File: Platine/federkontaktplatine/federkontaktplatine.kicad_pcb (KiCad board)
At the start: 2 copper layers, 256 x 149 mm, 15 parts, among them J1 Conn_01x07

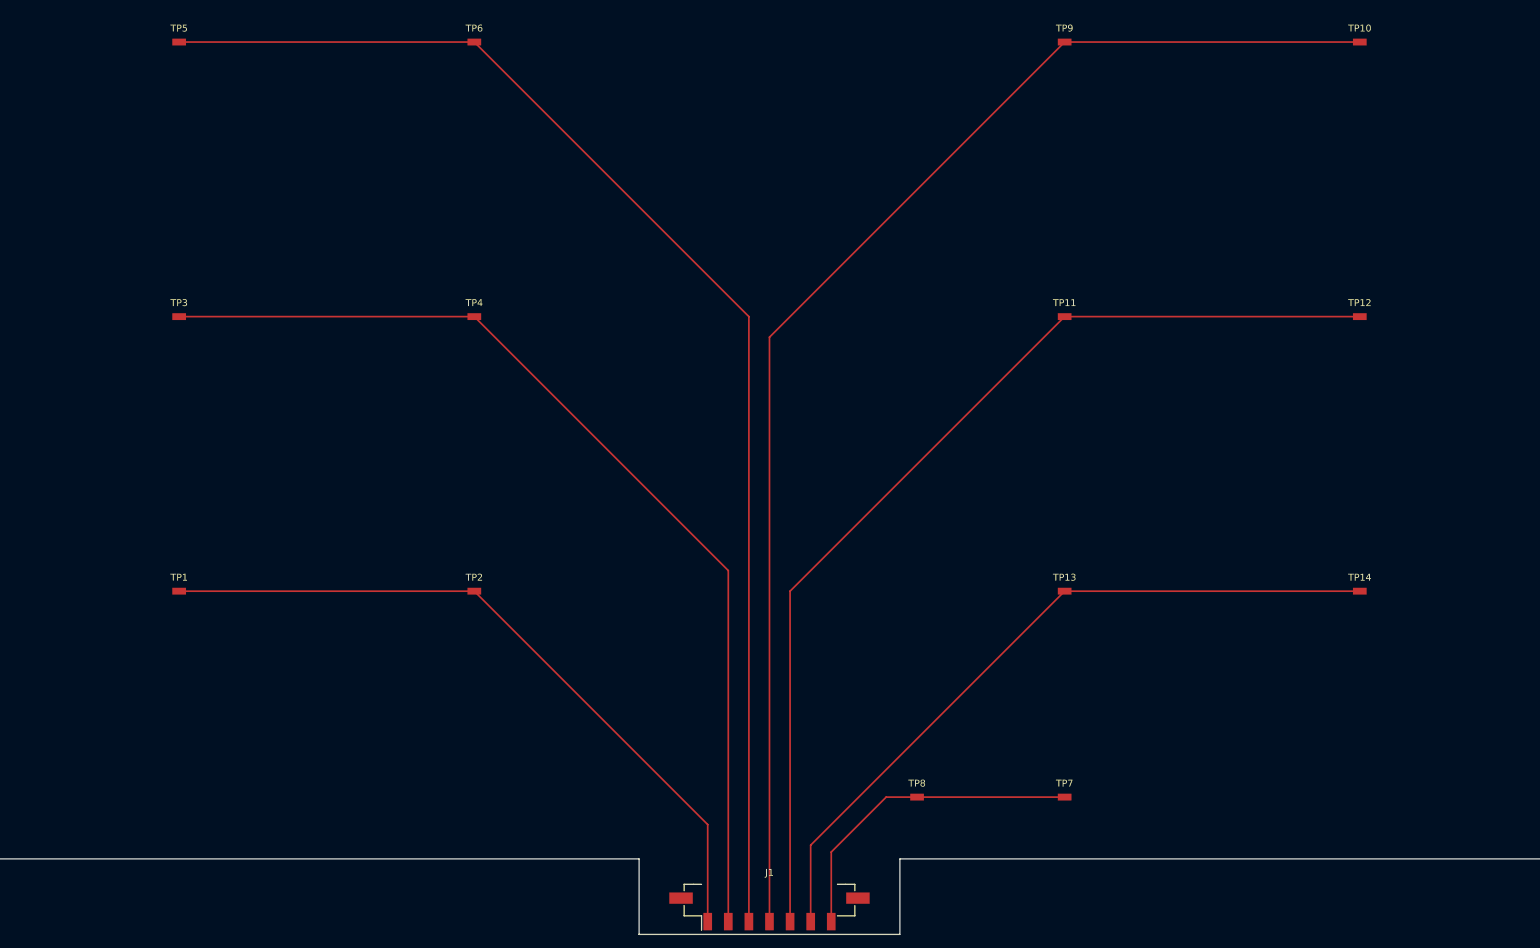
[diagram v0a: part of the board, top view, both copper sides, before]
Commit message: montagepunkte untere platine
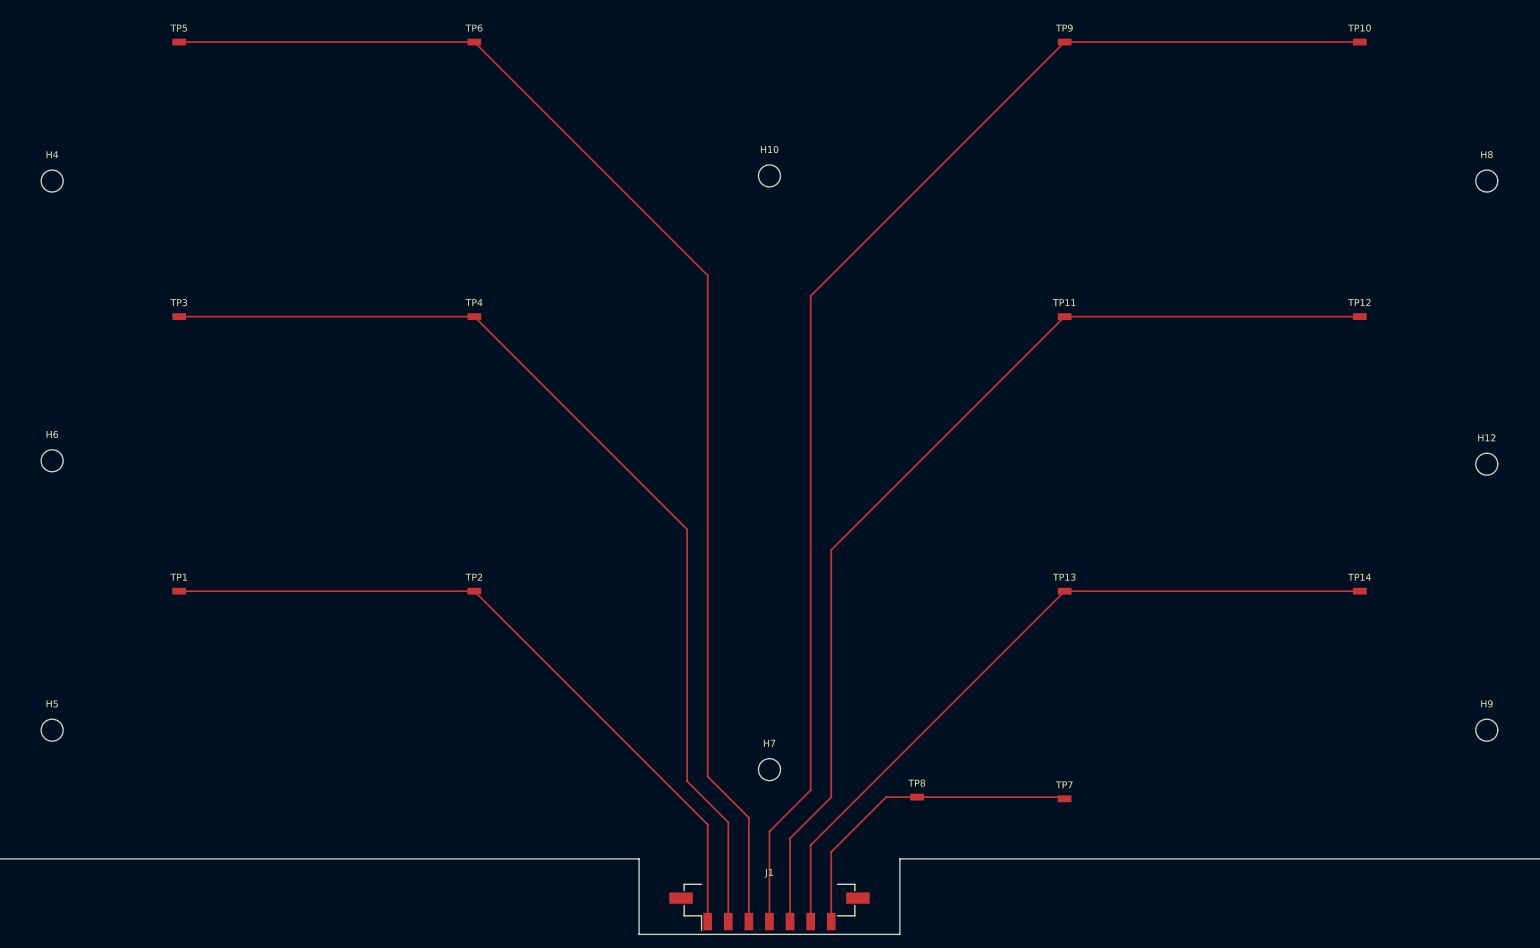
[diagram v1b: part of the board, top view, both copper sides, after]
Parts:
- added H10: MountingHole, MountingHole:MountingHole_3.2mm_M3_DIN965, F.Cu at (148.0, 58.5)
- added H12: MountingHole, MountingHole:MountingHole_3.2mm_M3_DIN965, F.Cu at (252.5, 100.5)
- added H4: MountingHole, MountingHole:MountingHole_3.2mm_M3_DIN965, F.Cu at (43.5, 59.2)
- added H5: MountingHole, MountingHole:MountingHole_3.2mm_M3_DIN965, F.Cu at (43.5, 139.2)
- added H6: MountingHole, MountingHole:MountingHole_3.2mm_M3_DIN965, F.Cu at (43.5, 100.0)
- added H7: MountingHole, MountingHole:MountingHole_3.2mm_M3_DIN965, F.Cu at (148.0, 145.0)
- added H8: MountingHole, MountingHole:MountingHole_3.2mm_M3_DIN965, F.Cu at (252.5, 59.2)
- added H9: MountingHole, MountingHole:MountingHole_3.2mm_M3_DIN965, F.Cu at (252.5, 139.2)
- moved TP7 0.25 mm to (191.0, 149.2)

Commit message: montagelöcher untere platte
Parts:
- added H1: MountingHole, MountingHole:MountingHole_3.2mm_M3_DIN965, F.Cu at (148.0, 19.2)
- added H2: MountingHole, MountingHole:MountingHole_3.2mm_M3_DIN965, F.Cu at (148.0, 99.2)
- moved H7 7.00 mm to (148.0, 138.0)
- moved H12 1.25 mm to (252.5, 99.2)
- moved H10 0.75 mm to (148.0, 59.2)
- moved H6 0.75 mm to (43.5, 99.2)
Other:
- board size 256 x 149 mm -> 256 x 153.8 mm
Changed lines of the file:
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@@
   (net 7 "Net-(J1-Pin_7)")
   (footprint "MountingHole:MountingHole_3.2mm_M3_DIN965" (layer "F.Cu")
-    (at 43.5 100)
+    (at 43.5 99.25)
     (descr "Mounting Hole 3.2mm, no annular, M3, DIN965")
     (tags "mounting hole 3.2mm no annular m3 din965")
@@
     (pad "" np_thru_hole circle (at 0 0) (size 3.2 3.2) (drill 3.2) (layers "*.Cu" "*.Mask"))
   )
+  (footprint "MountingHole:MountingHole_3.2mm_M3_DIN965" (layer "F.Cu")
+    (at 148 99.25)
+    (descr "Mounting Hole 3.2mm, no annular, M3, DIN965")
+    (tags "mounting hole 3.2mm no annular m3 din965")
+    (property "Sheetfile" "federkontaktplatine.kicad_sch")
+    (property "Sheetname" "")
+    (property "ki_description" "Mounting Hole without connection")
+    (property "ki_keywords" "mounting hole")
+    (attr exclude_from_pos_files)
+    (fp_text reference "H2" (at 0 -3.8) (layer "F.SilkS")
+        (effects (font (size 1 1) (thickness 0.15)))
+    )
+    (fp_text value "MountingHole" (at 0 3.8) (layer "F.Fab")
+        (effects (font (size 1 1) (thickness 0.15)))
+    )
+    (fp_text user "${REFERENCE}" (at 0 0) (layer "F.Fab")
+        (effects (font (size 1 1) (thickness 0.15)))
+    )
+    (fp_circle (center 0 0) (end 2.8 0)
+      (stroke (width 0.15) (type solid)) (fill none) (layer "Cmts.User"))
+    (fp_circle (center 0 0) (end 3.05 0)
+      (stroke (width 0.05) (type solid)) (fill none) (layer "F.CrtYd"))
+    (pad "" np_thru_hole circle (at 0 0) (size 3.2 3.2) (drill 3.2) (layers "*.Cu" "*.Mask"))
+  )
   (footprint "TestPoint:PAD_1x2mm" (layer "F.Cu")
     (at 191 79)
@@
   )
   (footprint "MountingHole:MountingHole_3.2mm_M3_DIN965" (layer "F.Cu")
-    (at 148 58.5)
+    (at 148 19.25)
+    (descr "Mounting Hole 3.2mm, no annular, M3, DIN965")
+    (tags "mounting hole 3.2mm no annular m3 din965")
+    (property "Sheetfile" "federkontaktplatine.kicad_sch")
+    (property "Sheetname" "")
+    (property "ki_description" "Mounting Hole without connection")
+    (property "ki_keywords" "mounting hole")
+    (attr exclude_from_pos_files)
+    (fp_text reference "H1" (at 0 4.25) (layer "F.SilkS")
+        (effects (font (size 1 1) (thickness 0.15)))
+    )
+    (fp_text value "MountingHole" (at 0 5.75) (layer "F.Fab")
+        (effects (font (size 1 1) (thickness 0.15)))
+    )
+    (fp_text user "${REFERENCE}" (at 0 0) (layer "F.Fab")
+        (effects (font (size 1 1) (thickness 0.15)))
+    )
+    (fp_circle (center 0 0) (end 2.8 0)
+      (stroke (width 0.15) (type solid)) (fill none) (layer "Cmts.User"))
+    (fp_circle (center 0 0) (end 3.05 0)
+      (stroke (width 0.05) (type solid)) (fill none) (layer "F.CrtYd"))
+    (pad "" np_thru_hole circle (at 0 0) (size 3.2 3.2) (drill 3.2) (layers "*.Cu" "*.Mask"))
+  )
+  (footprint "MountingHole:MountingHole_3.2mm_M3_DIN965" (layer "F.Cu")
+    (at 148 59.25)
     (descr "Mounting Hole 3.2mm, no annular, M3, DIN965")
     (tags "mounting hole 3.2mm no annular m3 din965")
@@
   )
   (footprint "MountingHole:MountingHole_3.2mm_M3_DIN965" (layer "F.Cu")
-    (at 148 145)
+    (at 148 138)
     (descr "Mounting Hole 3.2mm, no annular, M3, DIN965")
     (tags "mounting hole 3.2mm no annular m3 din965")
@@
   )
   (footprint "MountingHole:MountingHole_3.2mm_M3_DIN965" (layer "F.Cu")
-    (at 252.5 100.5)
+    (at 252.5 99.25)
     (descr "Mounting Hole 3.2mm, no annular, M3, DIN965")
     (tags "mounting hole 3.2mm no annular m3 din965")
@@
     (pad "" np_thru_hole circle (at 0 0) (size 3.2 3.2) (drill 3.2) (layers "*.Cu" "*.Mask"))
   )
-  (gr_arc (start 20 25) (mid 21.464466 21.464466) (end 25 20)
-    (stroke (width 0.1) (type default)) (layer "Edge.Cuts"))
   (gr_arc (start 25 158) (mid 21.464466 156.535534) (end 20 153)
     (stroke (width 0.1) (type default)) (layer "Edge.Cuts"))
-  (gr_line (start 20 25) (end 20 153)
+  (gr_line (start 144 19.25) (end 144 20.5)
+    (stroke (width 0.1) (type default)) (layer "Edge.Cuts"))
+  (gr_line (start 20.000001 25.5) (end 20 153)
     (stroke (width 0.1) (type default)) (layer "Edge.Cuts"))
   (gr_line (start 129 169) (end 167 169)
@@
   (gr_line (start 129 158) (end 25 158)
     (stroke (width 0.1) (type default)) (layer "Edge.Cuts"))
+  (gr_arc (start 20.000001 25.5) (mid 21.464467 21.964467) (end 25 20.500001)
+    (stroke (width 0.1) (type default)) (layer "Edge.Cuts"))
   (gr_line (start 167 158) (end 271 158)
     (stroke (width 0.1) (type default)) (layer "Edge.Cuts"))
-  (gr_line (start 276 153) (end 276 25)
+  (gr_arc (start 144 19.25) (mid 148 15.25) (end 152 19.25)
+    (stroke (width 0.1) (type default)) (layer "Edge.Cuts"))
+  (gr_line (start 276 153) (end 276 25.5)
     (stroke (width 0.1) (type default)) (layer "Edge.Cuts"))
   (gr_line (start 167 169) (end 167 158)
     (stroke (width 0.1) (type default)) (layer "Edge.Cuts"))
-  (gr_line (start 25 20) (end 271 20)
-    (stroke (width 0.1) (type default)) (layer "Edge.Cuts"))
-  (gr_arc (start 271 20) (mid 274.535534 21.464466) (end 276 25)
+  (gr_line (start 152 20.5) (end 271 20.5)
+    (stroke (width 0.1) (type default)) (layer "Edge.Cuts"))
+  (gr_line (start 25 20.5) (end 144 20.5)
+    (stroke (width 0.1) (type default)) (layer "Edge.Cuts"))
+  (gr_arc (start 271 20.5) (mid 274.535534 21.964466) (end 276 25.5)
     (stroke (width 0.1) (type default)) (layer "Edge.Cuts"))
   (gr_line (start 129 158) (end 129 169)
@@
   (gr_arc (start 276 153) (mid 274.535534 156.535534) (end 271 158)
     (stroke (width 0.1) (type default)) (layer "Edge.Cuts"))
+  (gr_line (start 152 19.25) (end 152 20.5)
+    (stroke (width 0.1) (type default)) (layer "Edge.Cuts"))
   (segment (start 139 153) (end 105 119) (width 0.25) (layer "F.Cu") (net 1))
-  (segment (start 105 119) (end 62 119) (width 0.25) (layer "F.Cu") (net 1))
   (segment (start 139 167.135) (end 139 153) (width 0.25) (layer "F.Cu") (net 1))
-  (segment (start 136 110) (end 105 79) (width 0.25) (layer "F.Cu") (net 2))
-  (segment (start 142 152.681802) (end 136 146.681802) (width 0.25) (layer "F.Cu") (net 2))
-  (segment (start 62 79) (end 105 79) (width 0.25) (layer "F.Cu") (net 2))
-  (segment (start 136 146.681802) (end 136 110) (width 0.25) (layer "F.Cu") (net 2))
+  (segment (start 105 119.25) (end 62 119.25) (width 0.25) (layer "F.Cu") (net 1))
+  (segment (start 139 113) (end 105 79) (width 0.25) (layer "F.Cu") (net 2))
   (segment (start 142 167.135) (end 142 152.681802) (width 0.25) (layer "F.Cu") (net 2))
+  (segment (start 139 149.681802) (end 139 113) (width 0.25) (layer "F.Cu") (net 2))
+  (segment (start 62 79.25) (end 105 79.25) (width 0.25) (layer "F.Cu") (net 2))
+  (segment (start 142 152.681802) (end 139 149.681802) (width 0.25) (layer "F.Cu") (net 2))
+  (segment (start 142 76) (end 105 39) (width 0.25) (layer "F.Cu") (net 3))
+  (segment (start 145 152) (end 142 149) (width 0.25) (layer "F.Cu") (net 3))
   (segment (start 145 167.135) (end 145 152) (width 0.25) (layer "F.Cu") (net 3))
-  (segment (start 139 73) (end 105 39) (width 0.25) (layer "F.Cu") (net 3))
-  (segment (start 145 152) (end 139 146) (width 0.25) (layer "F.Cu") (net 3))
-  (segment (start 139 146) (end 139 73) (width 0.25) (layer "F.Cu") (net 3))
-  (segment (start 105 39) (end 62 39) (width 0.25) (layer "F.Cu") (net 3))
+  (segment (start 105 39.25) (end 62 39.25) (width 0.25) (layer "F.Cu") (net 3))
+  (segment (start 142 149) (end 142 76) (width 0.25) (layer "F.Cu") (net 3))
   (segment (start 191 39) (end 154 76) (width 0.25) (layer "F.Cu") (net 4))
   (segment (start 154 76) (end 154 148) (width 0.25) (layer "F.Cu") (net 4))
-  (segment (start 234 39) (end 191 39) (width 0.25) (layer "F.Cu") (net 4))
+  (segment (start 234 39.25) (end 191 39.25) (width 0.25) (layer "F.Cu") (net 4))
   (segment (start 154 148) (end 148 154) (width 0.25) (layer "F.Cu") (net 4))
   (segment (start 148 154) (end 148 167.135) (width 0.25) (layer "F.Cu") (net 4))
+  (segment (start 151 155) (end 151 167.135) (width 0.25) (layer "F.Cu") (net 5))
+  (segment (start 234 79.25) (end 191 79.25) (width 0.25) (layer "F.Cu") (net 5))
   (segment (start 157 113) (end 157 149) (width 0.25) (layer "F.Cu") (net 5))
-  (segment (start 234 79) (end 191 79) (width 0.25) (layer "F.Cu") (net 5))
   (segment (start 191 79) (end 157 113) (width 0.25) (layer "F.Cu") (net 5))
   (segment (start 157 149) (end 151 155) (width 0.25) (layer "F.Cu") (net 5))
-  (segment (start 151 155) (end 151 167.135) (width 0.25) (layer "F.Cu") (net 5))
   (segment (start 191 119) (end 154 156) (width 0.25) (layer "F.Cu") (net 6))
-  (segment (start 234 119) (end 191 119) (width 0.25) (layer "F.Cu") (net 6))
   (segment (start 154 156) (end 154 167.135) (width 0.25) (layer "F.Cu") (net 6))
-  (segment (start 191 149) (end 169.5 149) (width 0.25) (layer "F.Cu") (net 7))
-  (segment (start 165 149) (end 169.5 149) (width 0.25) (layer "F.Cu") (net 7))
-  (segment (start 157 157) (end 165 149) (width 0.25) (layer "F.Cu") (net 7))
-  (segment (start 157 167.135) (end 157 157) (width 0.25) (layer "F.Cu") (net 7))
+  (segment (start 234 119.25) (end 191 119.25) (width 0.25) (layer "F.Cu") (net 6))
+  (segment (start 191 149.25) (end 169.5 149.25) (width 0.25) (layer "F.Cu") (net 7))
+  (segment (start 165 149.25) (end 169.5 149.25) (width 0.25) (layer "F.Cu") (net 7))
+  (segment (start 157 157.25) (end 165 149.25) (width 0.25) (layer "F.Cu") (net 7))
+  (segment (start 157 167) (end 157 157.25) (width 0.25) (layer "F.Cu") (net 7))
 )

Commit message: Kabelstrang
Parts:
- moved H12 20.2 mm to (255.5, 79.2)
- moved H4 20.2 mm to (40.5, 39.2)
- moved H5 20.2 mm to (40.5, 119.2)
- moved H6 20.2 mm to (40.5, 79.2)
- moved H8 20.2 mm to (255.5, 39.2)
- moved H9 20.2 mm to (255.5, 119.2)
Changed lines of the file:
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@@
   (net 7 "Net-(J1-Pin_7)")
   (footprint "MountingHole:MountingHole_3.2mm_M3_DIN965" (layer "F.Cu")
-    (at 43.5 99.25)
+    (at 40.5 79.25)
     (descr "Mounting Hole 3.2mm, no annular, M3, DIN965")
     (tags "mounting hole 3.2mm no annular m3 din965")
@@
   )
   (footprint "MountingHole:MountingHole_3.2mm_M3_DIN965" (layer "F.Cu")
-    (at 252.5 139.25)
+    (at 255.5 119.25)
     (descr "Mounting Hole 3.2mm, no annular, M3, DIN965")
     (tags "mounting hole 3.2mm no annular m3 din965")
@@
   )
   (footprint "MountingHole:MountingHole_3.2mm_M3_DIN965" (layer "F.Cu")
-    (at 43.5 139.25)
+    (at 40.5 119.25)
     (descr "Mounting Hole 3.2mm, no annular, M3, DIN965")
     (tags "mounting hole 3.2mm no annular m3 din965")
@@
   )
   (footprint "MountingHole:MountingHole_3.2mm_M3_DIN965" (layer "F.Cu")
-    (at 252.5 59.25)
+    (at 255.5 39.25)
     (descr "Mounting Hole 3.2mm, no annular, M3, DIN965")
     (tags "mounting hole 3.2mm no annular m3 din965")
@@
   )
   (footprint "MountingHole:MountingHole_3.2mm_M3_DIN965" (layer "F.Cu")
-    (at 252.5 99.25)
+    (at 255.5 79.25)
     (descr "Mounting Hole 3.2mm, no annular, M3, DIN965")
     (tags "mounting hole 3.2mm no annular m3 din965")
@@
   )
   (footprint "MountingHole:MountingHole_3.2mm_M3_DIN965" (layer "F.Cu")
-    (at 43.5 59.25)
+    (at 40.5 39.25)
     (descr "Mounting Hole 3.2mm, no annular, M3, DIN965")
     (tags "mounting hole 3.2mm no annular m3 din965")
@@
   (gr_line (start 276 153) (end 276 25.5)
     (stroke (width 0.1) (type default)) (layer "Edge.Cuts"))
+  (gr_line (start 25 20.5) (end 144 20.5)
+    (stroke (width 0.1) (type default)) (layer "Edge.Cuts"))
   (gr_line (start 167 169) (end 167 158)
     (stroke (width 0.1) (type default)) (layer "Edge.Cuts"))
   (gr_line (start 152 20.5) (end 271 20.5)
     (stroke (width 0.1) (type default)) (layer "Edge.Cuts"))
-  (gr_line (start 25 20.5) (end 144 20.5)
-    (stroke (width 0.1) (type default)) (layer "Edge.Cuts"))
   (gr_arc (start 271 20.5) (mid 274.535534 21.964466) (end 276 25.5)
